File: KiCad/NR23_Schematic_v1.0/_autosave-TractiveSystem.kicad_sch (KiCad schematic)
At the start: 9 parts, among them M1 Zero_7R_Motor

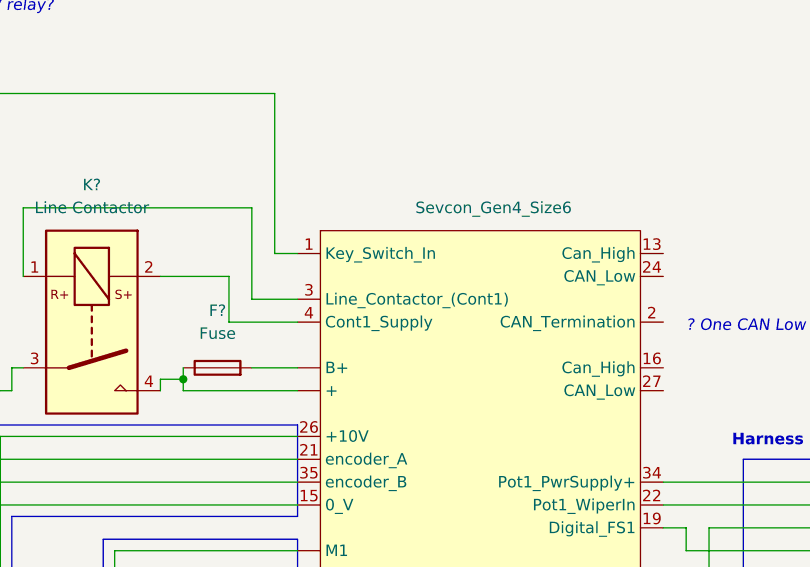
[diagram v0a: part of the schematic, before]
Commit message: keyswitch
updated key switch to be pin 6. did other things
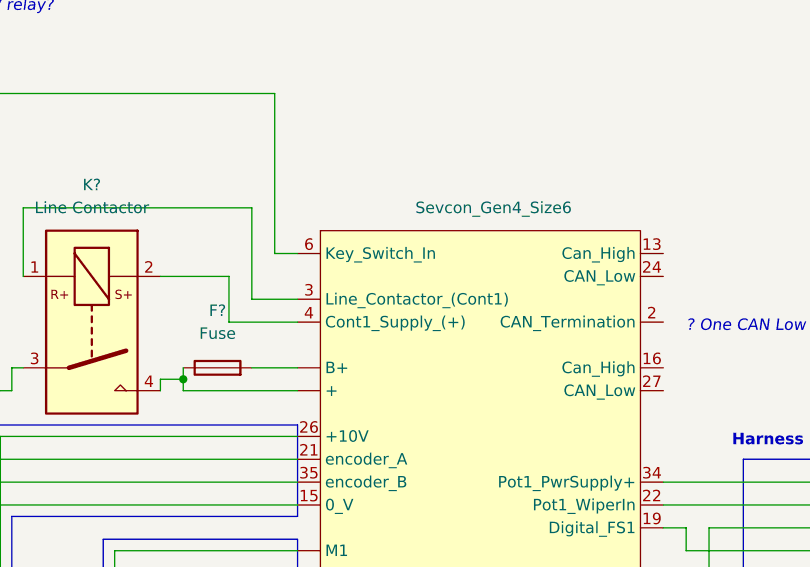
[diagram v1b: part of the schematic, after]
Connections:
- net at U?. (M3): now also F?.2
- net at SW?.2 (B): now also U?.6 (Key_Switch_In); no longer U?.1 (Key_Switch_In)
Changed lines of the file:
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@@
     )
     (property "Footprint" "" (id 2) (at 119.38 130.81 0)
-      (effects (font (size 1.27 1.27)) hide)
+      (effects (font (size 1.27 1.27) italic) hide)
     )
     (property "Datasheet" "" (id 3) (at 119.38 130.81 0)
@@
     (pin "")
     (pin "")
-    (pin "1")
     (pin "13")
     (pin "15")
@@
     (pin "35")
     (pin "4")
+    (pin "6")
   )
   (symbol (lib_id "Device:R") (at 217.17 125.73 90) (unit 1)
